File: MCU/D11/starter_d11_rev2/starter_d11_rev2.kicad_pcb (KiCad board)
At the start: 2 copper layers, 36.3 x 48.5 mm, 23 parts, among them J1 USB_A, J1A USB, J2 SWD-5, J3 Data, J4 out_5V0, J5 out_3V3, SW1 Reset, U1 ATSAMD11C14A-SS, U2 PRTR5V0, U3 TLV73333/SOT-23, X1 ECS-2520MV-xxx-xx

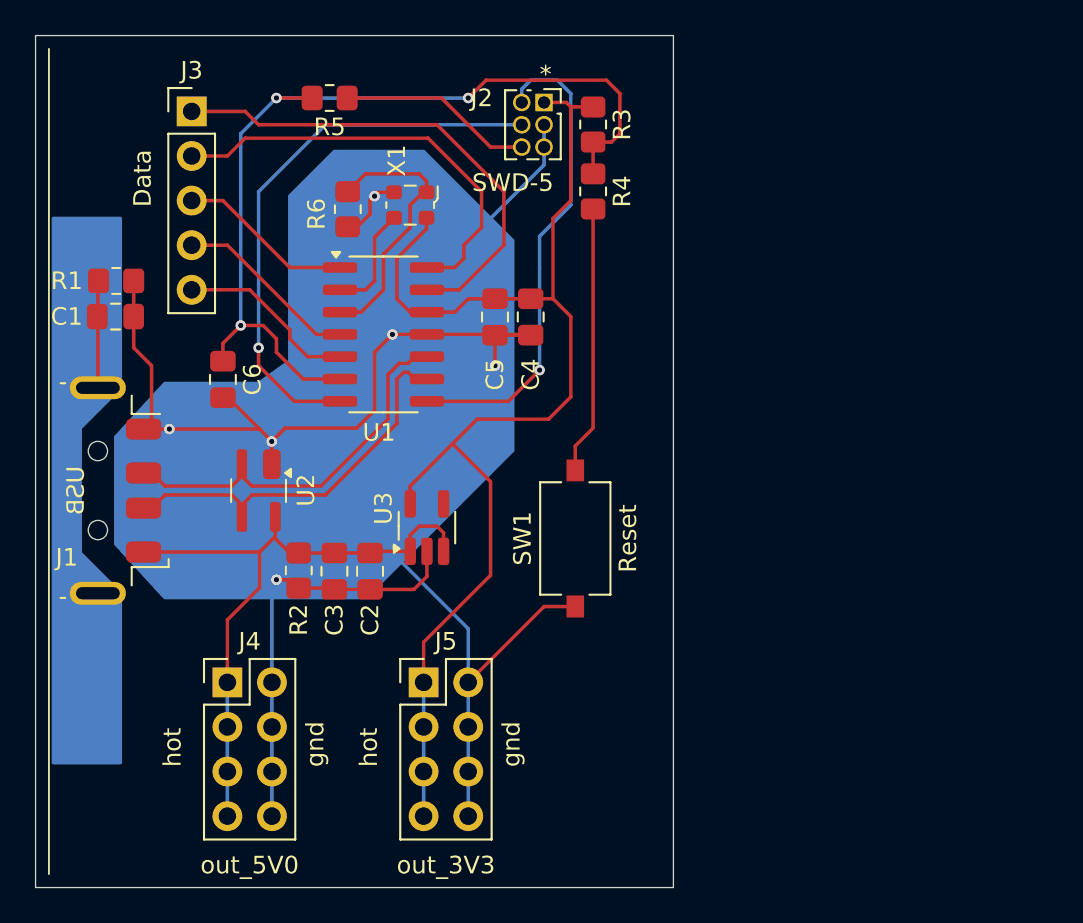
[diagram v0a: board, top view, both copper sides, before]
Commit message: D11 schematics and PCB updates - printed prototype version
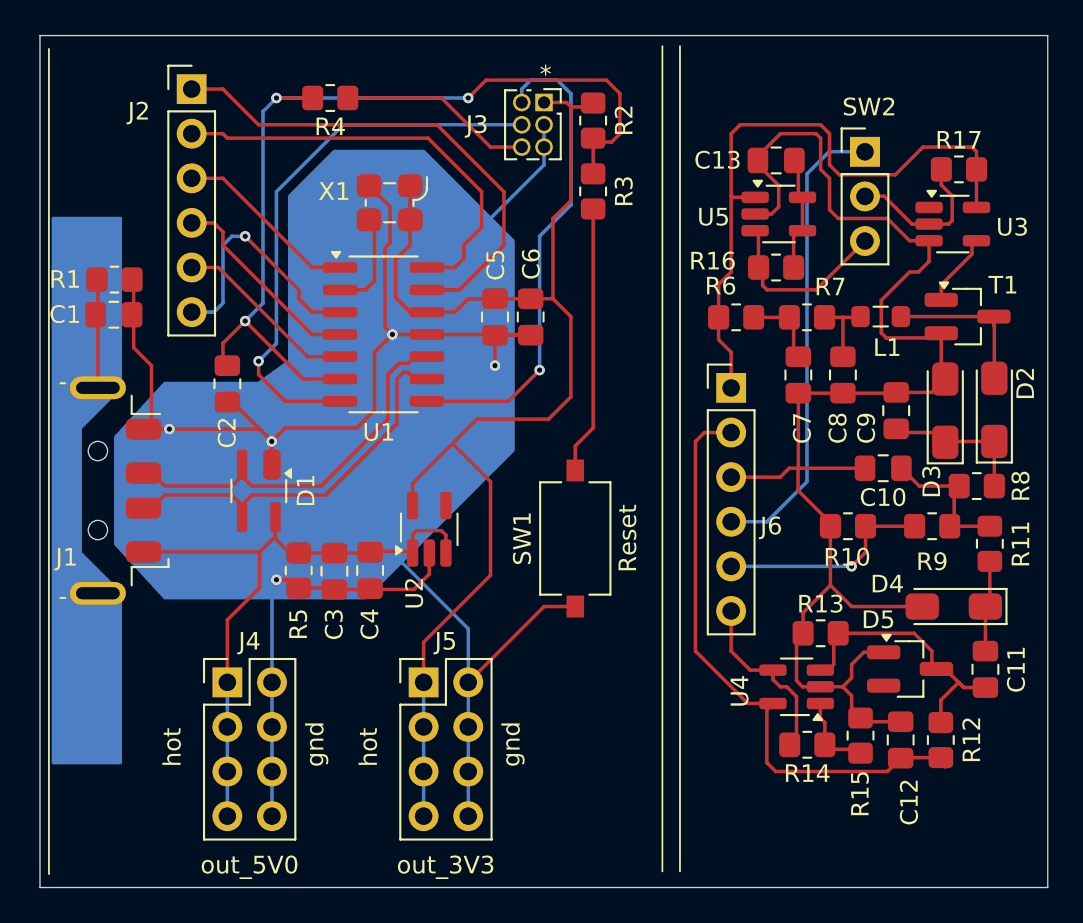
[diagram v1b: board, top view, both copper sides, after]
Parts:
- added C10: 1µ, Capacitor_SMD:C_0805_2012Metric_Pad1.18x1.45mm_HandSolder, F.Cu at (131.1, 82.0)
- added C11: 0.01µ, Capacitor_SMD:C_0805_2012Metric_Pad1.18x1.45mm_HandSolder, F.Cu at (136.9, 93.5)
- added C12: 0.1µ, Capacitor_SMD:C_0805_2012Metric_Pad1.18x1.45mm_HandSolder, F.Cu at (132.1, 97.5)
- added C13: 2.2µ, Capacitor_SMD:C_0805_2012Metric_Pad1.18x1.45mm_HandSolder, F.Cu at (125.0, 64.5)
- added C7: 2.2µ, Capacitor_SMD:C_0805_2012Metric_Pad1.18x1.45mm_HandSolder, F.Cu at (126.2, 76.7)
- added C8: 2.2µ, Capacitor_SMD:C_0805_2012Metric_Pad1.18x1.45mm_HandSolder, F.Cu at (128.8, 76.7)
- added C9: 1µ, Capacitor_SMD:C_0805_2012Metric_Pad1.18x1.45mm_HandSolder, F.Cu at (131.8, 78.8)
- added D1: PRTR5V0, Package_TO_SOT_SMD:SOT-143_Handsoldering, F.Cu at (95.5, 83.3)
- added D2: 1N4007, Secoh:D_SOD-123F_hand_soldering, F.Cu at (137.4, 78.7)
- added D3: SMF36A, Secoh:D_SOD-123F_hand_soldering, F.Cu at (134.6, 78.8)
- added D4: SMF24A, Secoh:D_SOD-123F_hand_soldering, F.Cu at (135.1, 89.9)
- added D5: MMBZ5222BLT1G, Package_TO_SOT_SMD:SOT-23_Handsoldering, F.Cu at (132.6, 93.5)
- added J6: Conn_01x06_Pin, Connector_PinHeader_2.54mm:PinHeader_1x06_P2.54mm_Vertical, F.Cu at (122.4, 77.5)
- added L1: 100µ, Inductor_SMD:L_0805_2012Metric_Pad1.05x1.20mm_HandSolder, F.Cu at (130.9, 73.4)
- added R10: 10k, Resistor_SMD:R_0805_2012Metric_Pad1.20x1.40mm_HandSolder, F.Cu at (129.1, 85.3)
- added R11: 100k, Resistor_SMD:R_0805_2012Metric_Pad1.20x1.40mm_HandSolder, F.Cu at (137.1, 86.3)
- added R12: 1Meg, Resistor_SMD:R_0805_2012Metric_Pad1.20x1.40mm_HandSolder, F.Cu at (134.4, 97.5)
- added R13: 47k, Resistor_SMD:R_0805_2012Metric_Pad1.20x1.40mm_HandSolder, F.Cu at (127.5, 91.4)
- added R14: 100k, Resistor_SMD:R_0805_2012Metric_Pad1.20x1.40mm_HandSolder, F.Cu at (126.7, 97.8)
- added R15: 10k, Resistor_SMD:R_0805_2012Metric_Pad1.20x1.40mm_HandSolder, F.Cu at (129.8, 97.3)
- added R16: 180, Resistor_SMD:R_0805_2012Metric_Pad1.20x1.40mm_HandSolder, F.Cu at (125.0, 70.6)
- added R17: 100k, Resistor_SMD:R_0805_2012Metric_Pad1.20x1.40mm_HandSolder, F.Cu at (135.4, 65.0)
- added R7: 33, Resistor_SMD:R_0805_2012Metric_Pad1.20x1.40mm_HandSolder, F.Cu at (126.7, 73.4)
- added R8: 10k, Resistor_SMD:R_0805_2012Metric_Pad1.20x1.40mm_HandSolder, F.Cu at (136.4, 83.1)
- added R9: 100k, Resistor_SMD:R_0805_2012Metric_Pad1.20x1.40mm_HandSolder, F.Cu at (133.9, 85.3)
- added SW2: Conn_01x03_Pin, Connector_PinHeader_2.54mm:PinHeader_1x03_P2.54mm_Vertical, F.Cu at (130.0, 64.0)
- added T1: 2N7002, Package_TO_SOT_SMD:SOT-23_Handsoldering, F.Cu at (135.9, 73.4)
- added U4: MAX4230, Package_TO_SOT_SMD:SOT-23-5_HandSoldering, F.Cu at (126.1, 94.5)
- added U5: MIC1555, Package_TO_SOT_SMD:SOT-23-5_HandSoldering, F.Cu at (125.1, 67.6)
- C2: value 100n -> 4.7n
- C3: value 4.7u -> 100n
- C5: value 100n -> 4.7u
- C6: value 4.7n -> 100n
- J1A: footprint Secoh:pad_single_005x03_in -> Secoh:pad_single_005x036in_for_USB_A
- J2: value SWD-5 -> Conn_01x06_Pin; footprint Connector_PinSocket_1.27mm:PinSocket_2x03_P1.27mm_Vertical -> Connector_PinHeader_2.54mm:PinHeader_1x06_P2.54mm_Vertical
- J3: value Data -> SWD-5; footprint Connector_PinHeader_2.54mm:PinHeader_1x05_P2.54mm_Vertical -> Connector_PinSocket_1.27mm:PinSocket_2x03_P1.27mm_Vertical
- R2: value 1M -> 100k
- R3: value 100k -> 39
- R5: value 39 -> 1M
- R6: value 10k -> 33
- U2: value PRTR5V0 -> TLV73333/SOT-23; footprint Package_TO_SOT_SMD:SOT-143_Handsoldering -> Package_TO_SOT_SMD:SOT-23-5_HandSoldering
- U3: value TLV73333/SOT-23 -> MC74VHC1GT14
- X1: footprint Oscillator:Oscillator_SMD_ECS_2520MV-xxx-xx-4Pin_2.5x2.0mm -> Secoh:ECS-2520MV
- moved U3 34.6 mm to (135.0, 68.1), turned to 0 degrees
- moved R2 30.6 mm to (114.6, 62.2)
- moved R5 27.0 mm to (97.8, 87.9), turned to -90 degrees
- moved R6 23.0 mm to (122.7, 73.4), turned to 180 degrees
- moved J2 20.1 mm to (91.7, 60.5)
- moved J3 20.1 mm to (111.8, 61.2)
- moved C6 17.9 mm to (111.0, 73.4)
- moved C4 17.1 mm to (101.9, 87.9)
- moved R4 15.9 mm to (99.6, 61.0), turned to 180 degrees
- moved C2 13.4 mm to (93.7, 77.2)
- moved U2 9.97 mm to (105.2, 85.5), turned to 90 degrees
- moved R3 3.81 mm to (114.6, 66.3)
- moved X1 1.30 mm to (102.8, 67.1)
- moved C1 0.14 mm to (87.3, 73.3)
- moved R1 0.12 mm to (87.3, 71.3)
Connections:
- net /CLK renamed /Inset A - USB MCU/CLK
- net /Shield renamed /Inset A - USB MCU/Shield
- C2 pad 1: 5V0 -> /Inset A - USB MCU/RST
- C4 pad 1: 3V3 -> 5V0
- C6 pad 1: /RST -> 3V3
- J1 pad 2: /USB-M -> /Inset A - USB MCU/USB-M
- J1 pad 3: /USB-P -> /Inset A - USB MCU/USB-P
- J2 pad 1: 3V3 -> Net-(J2-Pin_1)
- J2 pad 2: /SWDIO -> Net-(J2-Pin_2)
- J2 pad 3: GND -> Net-(J2-Pin_3)
- J2 pad 4: /SWCLK -> Net-(J2-Pin_4)
- J2 pad 5: GND -> Net-(J2-Pin_5)
- J3 pad 1: Net-(J3-Pin_1) -> 3V3
- J3 pad 2: Net-(J3-Pin_2) -> /Inset A - USB MCU/SWDIO
- J3 pad 3: Net-(J3-Pin_3) -> GND
- J3 pad 4: Net-(J3-Pin_4) -> /Inset A - USB MCU/SWCLK
- J3 pad 5: Net-(J3-Pin_5) -> GND
- R2 pad 1: 5V0 -> 3V3
- R2 pad 2: GND -> /Inset A - USB MCU/RST
- R3 pad 1: 3V3 -> /Inset A - USB MCU/RST
- R3 pad 2: /RST -> Net-(R3-Pad2)
- R4 pad 1: /RST -> Net-(J3-Pin_6)
- R4 pad 2: Net-(R4-Pad2) -> /Inset A - USB MCU/RST
- R5 pad 1: Net-(J2-Pin_6) -> 5V0
- R5 pad 2: /RST -> GND
- R6 pad 1: /CLK-EN -> Net-(C7-Pad1)
- R6 pad 2: GND -> 5V0-1
- SW1 pad 2: Net-(R4-Pad2) -> Net-(R3-Pad2)
- U1 pad 1: Net-(J3-Pin_3) -> Net-(J2-Pin_3)
- U1 pad 10: /USB-P -> /Inset A - USB MCU/USB-P
- U1 pad 13: Net-(J3-Pin_1) -> Net-(J2-Pin_1)
- U1 pad 14: Net-(J3-Pin_2) -> Net-(J2-Pin_2)
- U1 pad 3: /CLK-EN -> Net-(J2-Pin_6)
- U1 pad 4: Net-(J3-Pin_4) -> Net-(J2-Pin_4)
- U1 pad 5: Net-(J3-Pin_5) -> Net-(J2-Pin_5)
- U1 pad 6: /RST -> /Inset A - USB MCU/RST
- U1 pad 7: /SWCLK -> /Inset A - USB MCU/SWCLK
- U1 pad 8: /SWDIO -> /Inset A - USB MCU/SWDIO
- U1 pad 9: /USB-M -> /Inset A - USB MCU/USB-M
- U2 pad 1: GND -> 5V0
- U2 pad 2: /USB-P -> GND
- U2 pad 3: /USB-M -> 5V0
- U2 pad 4: 5V0 -> unconnected-(U2A-NC-Pad4)
- U3 pad 1: 5V0 -> unconnected-(U3-NC-Pad1)
- U3 pad 2: GND -> Net-(SW2-Pin_2)
- U3 pad 3: 5V0 -> GND1
- U3 pad 4: unconnected-(U3A-NC-Pad4) -> Net-(T1-G)
- U3 pad 5: 3V3 -> 5V0-1
- X1 pad 1: /CLK-EN -> 3V3
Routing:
- net GND1: track 0.00 -> 84.2 mm
- net /RST: track 51.8 -> 0.00 mm, vias 3 -> 0
- net /Inset A - USB MCU/RST: track 0.00 -> 51.2 mm, vias 0 -> 3
- net 5V0-1: track 0.00 -> 36.8 mm
- net 3V3-1: track 0.00 -> 34.1 mm
- net /SWCLK: track 31.9 -> 0.00 mm, vias 1 -> 0
- net /Inset A - USB MCU/SWCLK: track 0.00 -> 31.7 mm, vias 0 -> 1
- net Net-(J2-Pin_1): track 0.00 -> 28.7 mm
- net Net-(J3-Pin_1): track 28.2 -> 0.00 mm
- net /SWDIO: track 27.7 -> 0.00 mm, vias 1 -> 0
- net /Inset A - USB MCU/SWDIO: track 0.00 -> 27.7 mm, vias 0 -> 1
- net DRV: track 0.00 -> 26.6 mm
- net Net-(J3-Pin_2): track 24.7 -> 0.00 mm
- net Net-(J2-Pin_2): track 0.00 -> 24.4 mm
- net /USB-P: track 22.8 -> 0.00 mm
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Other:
- board size 36.3 x 48.5 mm -> 57.4 x 48.5 mm
